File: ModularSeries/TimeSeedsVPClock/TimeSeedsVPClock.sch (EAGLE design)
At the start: 51 parts

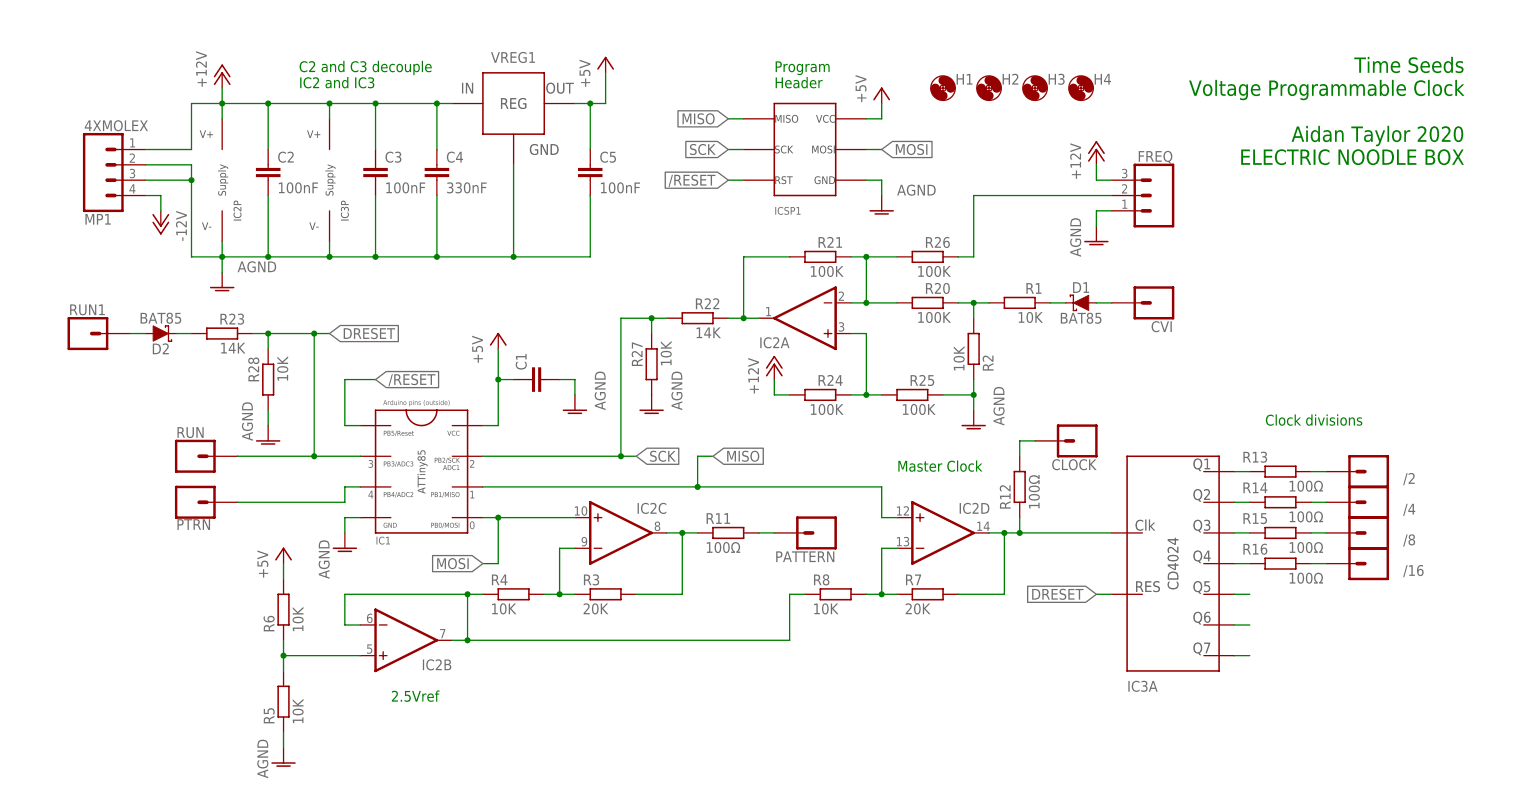
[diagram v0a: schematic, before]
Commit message: Schematic and layout added for Time Seeds and TRHP SVG
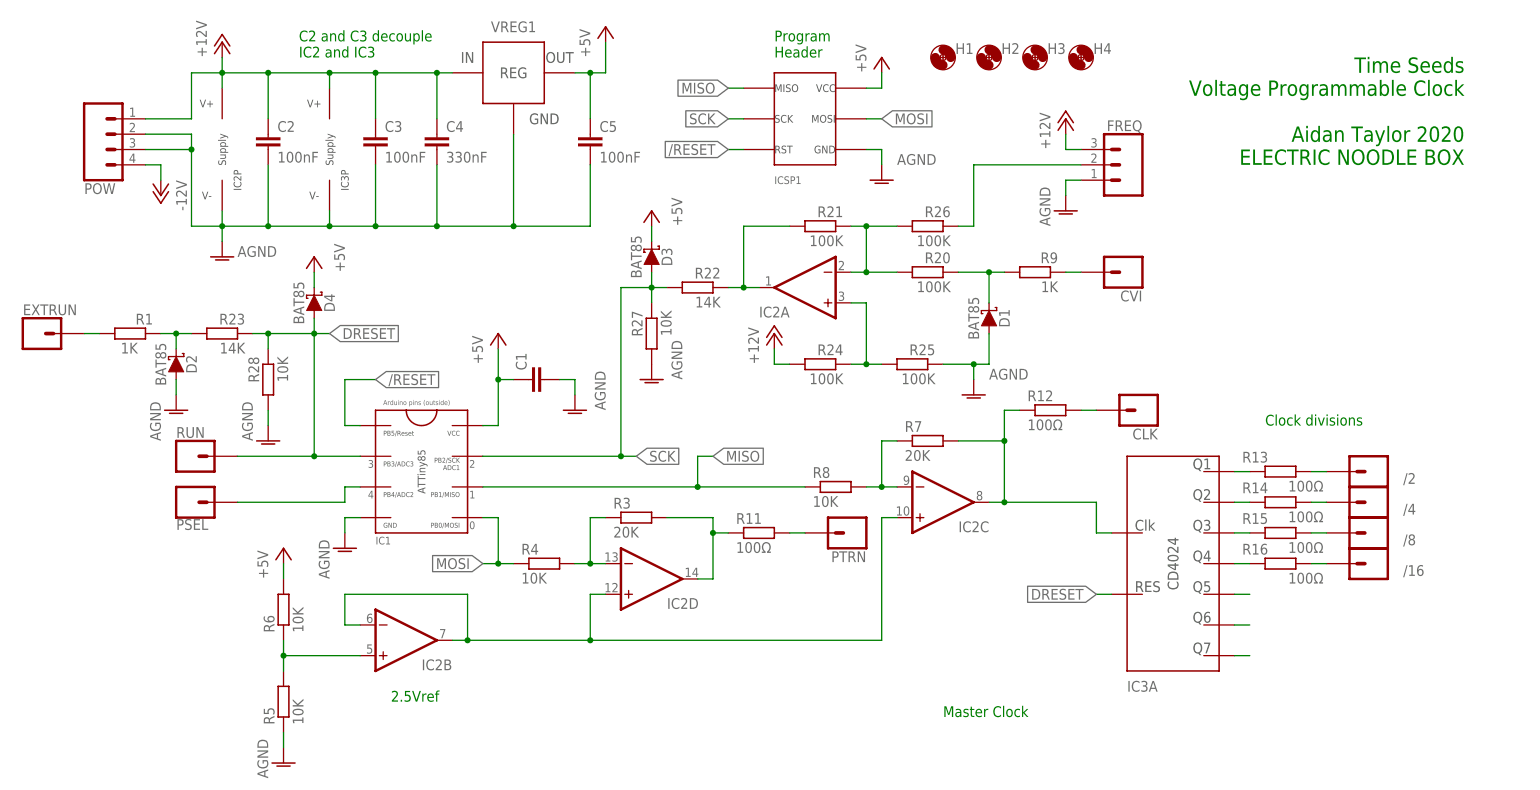
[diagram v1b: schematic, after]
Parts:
- removed CLOCK, PATTERN, RUN1: 1XWIREPAD, ElectricNoodleBox:1XWIREPAD
- removed MP1: 4XMOLEX, ElectricNoodleBox:4XMOLEX
- removed R2: 10K, rcl:R-EU_0207/10
- added CLK, EXTRUN, PSEL: 1XWIREPAD, ElectricNoodleBox:1XWIREPAD
- added D3, D4: BAT85, ElectricNoodleBox:SCHOTTKY_DO35
- added POW: 4XMOLEX, ElectricNoodleBox:4XMOLEX
- added R9: 1K, rcl:R-EU_0207/10
- IC2: device ElectricNoodleBox:TL0X4DIL -> ElectricNoodleBox:LM324
- R1: value 10K -> 1K
- VREG1: value L7805_TO-220 -> (none); device ElectricNoodleBox:L7805_TO-220 -> ElectricNoodleBox:L78L05TO92
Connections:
- removed net N$12: CLOCK.1, R12.2
- removed net N$26: D2.A, RUN1.1
- removed net N$28: D2.C, R23.2
- new net N$3: CVI.1, R9.1
- new net N$7: D2.C, R1.1, R23.2
- net +12V: now also POW.1; no longer MP1.1
- net +5V: now also D3.C, D4.C
- net -12V: now also POW.4; no longer MP1.4
- net AGND: now also D1.A, D2.A, POW.2, POW.3; no longer MP1.2, MP1.3, R2.1
- net DRESET: now also D4.A
- net MISO: now also R8.1; no longer IC2D.+IN
- net MOSI: now also R4.1; no longer IC2C.+IN
- net N$1: now also R20.1, R9.2; no longer R1.1
- net N$10: now also IC2C.+IN, IC2D.+IN; no longer R4.1, R8.1
- net N$11: now also PTRN.1; no longer PATTERN.1
- net N$2: now also EXTRUN.1; no longer R2.2, R20.1
- net N$23: now also CLK.1, R12.2; no longer CVI.1, D1.A
- net N$24: now also PSEL.1; no longer PTRN.1
- net N$4: now also IC2D.-IN; no longer IC2C.-IN
- net N$5: now also IC2D.OUT; no longer IC2C.OUT
- net N$8: now also IC2C.-IN; no longer IC2D.-IN
- net N$9: now also IC2C.OUT; no longer IC2D.OUT
- net SCK: now also D3.A
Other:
- moved on the sheet: C2, C3, C4, C5, CVI, D1, D2, FREQ, H1, H2, H3, H4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

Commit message: Time Seeds VPC and TRHP SVG op-amps, schematics and layouts updated
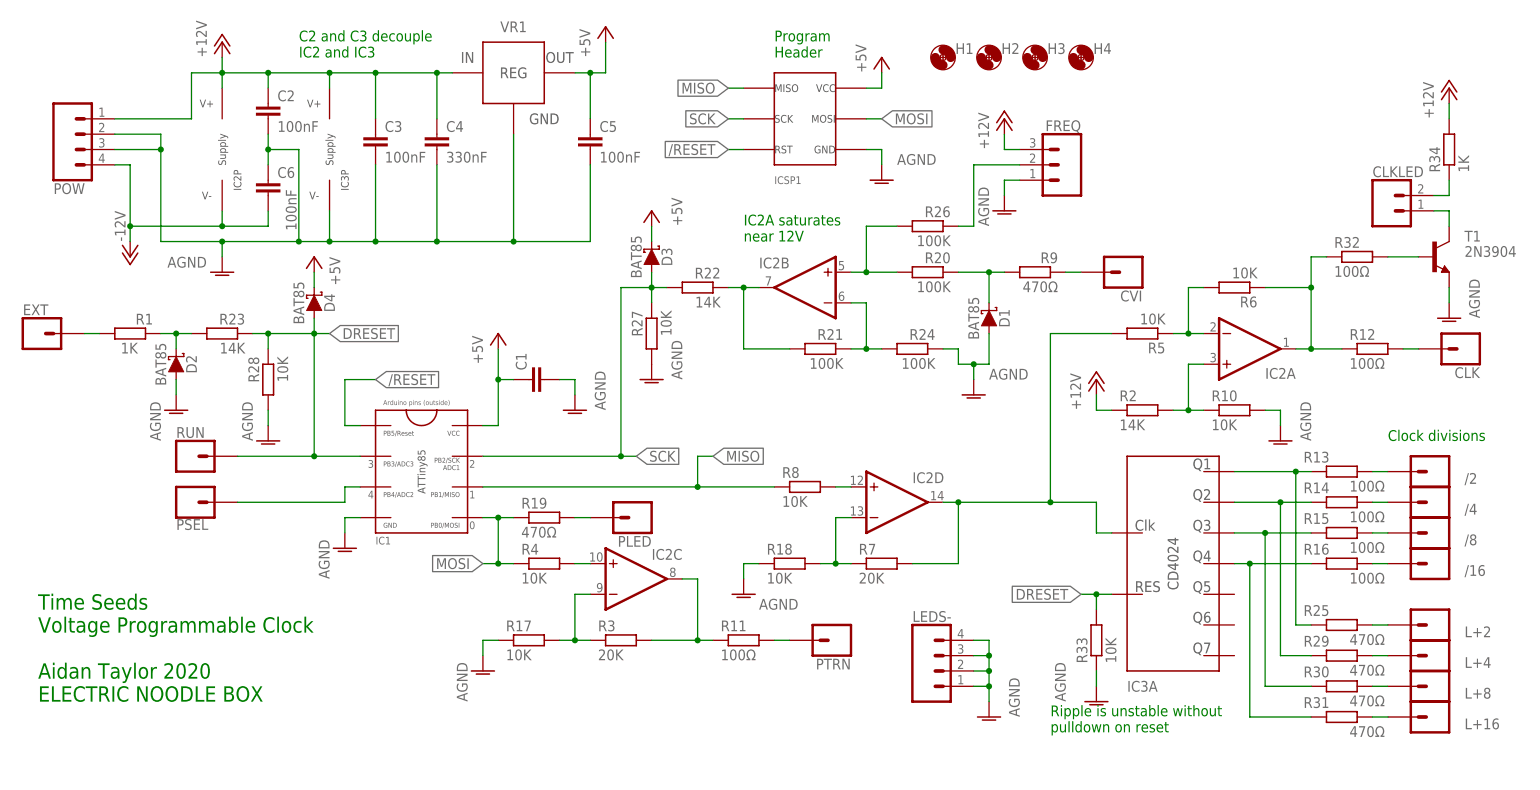
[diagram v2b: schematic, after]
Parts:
- added C6: 100nF, rcl:C-EU050-025X075
- added CLKLED: 2XWIREPAD, ElectricNoodleBox:2XWIREPAD
- added L+16, L+2, L+4, L+8, PLED: 1XWIREPAD, ElectricNoodleBox:1XWIREPAD
- added LEDS-: 4XWIREPAD, ElectricNoodleBox:4XWIREPAD
- added R10, R17, R18, R33: 10K, rcl:R-EU_0207/10
- added R19, R29, R30, R31: 470Ω, rcl:R-EU_0207/10
- added R2: 14K, rcl:R-EU_0207/10
- added R32: 100Ω, rcl:R-EU_0207/10
- added R34: 1K, rcl:R-EU_0207/10
- added T1: 2N3904, transistor:2N3904
- R25: value 100K -> 470Ω
- R9: value 1K -> 470Ω
- renumbered EXTRUN to EXT, VREG1 to VR1
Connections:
- new net N$12: IC2A.OUT, R12.1, R32.1, R6.1
- new net N$22: IC2A.+IN, R10.1, R2.2
- new net N$26: CLKLED.2, R34.1
- new net N$28: IC2D.-IN, R18.2, R7.1
- new net N$33: IC2D.OUT, IC3A.CLK, R5.2, R7.2
- new net N$34: L+16.1, R31.2
- new net N$35: CLKLED.1, T1.C
- new net N$36: R32.2, T1.B
- net +12V: now also R2.1, R34.2; no longer R24.2
- net +5V: no longer R6.2
- net -12V: now also C6.2, IC2P.V-
- net AGND: now also C6.1, LEDS-.1, LEDS-.2, LEDS-.3, LEDS-.4, R10.2, R17.1, R18.1, R24.1, R33.1, T1.E; no longer IC2P.V-, R25.1, R5.1
- net DRESET: now also R33.2
- net MOSI: now also R19.1
- net N$10: now also IC2C.OUT, R11.1, R3.2; no longer IC2B.-IN, IC2B.OUT, IC2C.+IN, IC2D.+IN
- net N$13: now also R25.1
- net N$14: now also R29.1
- net N$15: now also R30.1
- net N$16: now also R31.1
- net N$17: now also L+2.1, R25.2; no longer IC3A.Q5
- net N$18: now also L+4.1, R29.2; no longer IC3A.Q6
- net N$19: now also L+8.1, R30.2; no longer IC3A.Q7
- net N$20: now also IC2B.+IN; no longer IC2A.-IN, R21.1
- net N$21: now also IC2B.OUT; no longer IC2A.OUT
- net N$25: now also IC2B.-IN, R21.1, R24.2; no longer IC2A.+IN, R24.1, R25.2
- net N$4: now also IC2C.+IN; no longer IC2D.-IN, R3.1
- net N$5: now also IC2C.-IN, R17.2, R3.1; no longer IC2D.OUT, R11.1, R3.2
- net N$6: now also IC2A.-IN, R5.1, R6.2; no longer IC2B.+IN, R5.2, R6.1
- net N$8: now also IC2D.+IN; no longer IC2C.-IN, R7.1
- net N$9: now also PLED.1, R19.2; no longer IC2C.OUT, IC3A.CLK, R12.1, R7.2
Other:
- note added: "IC2A saturates near 12V"
- note added: "Ripple is unstable without pulldown on reset"
- note removed: "2.5Vref"
- note removed: "Master Clock"
- moved on the sheet: /16, /2, /4, /8, C2, CLK, FREQ, IC2A, IC2B, IC2C, IC2D, POW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

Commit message: CD4024 Reset fixed in Time Seeds
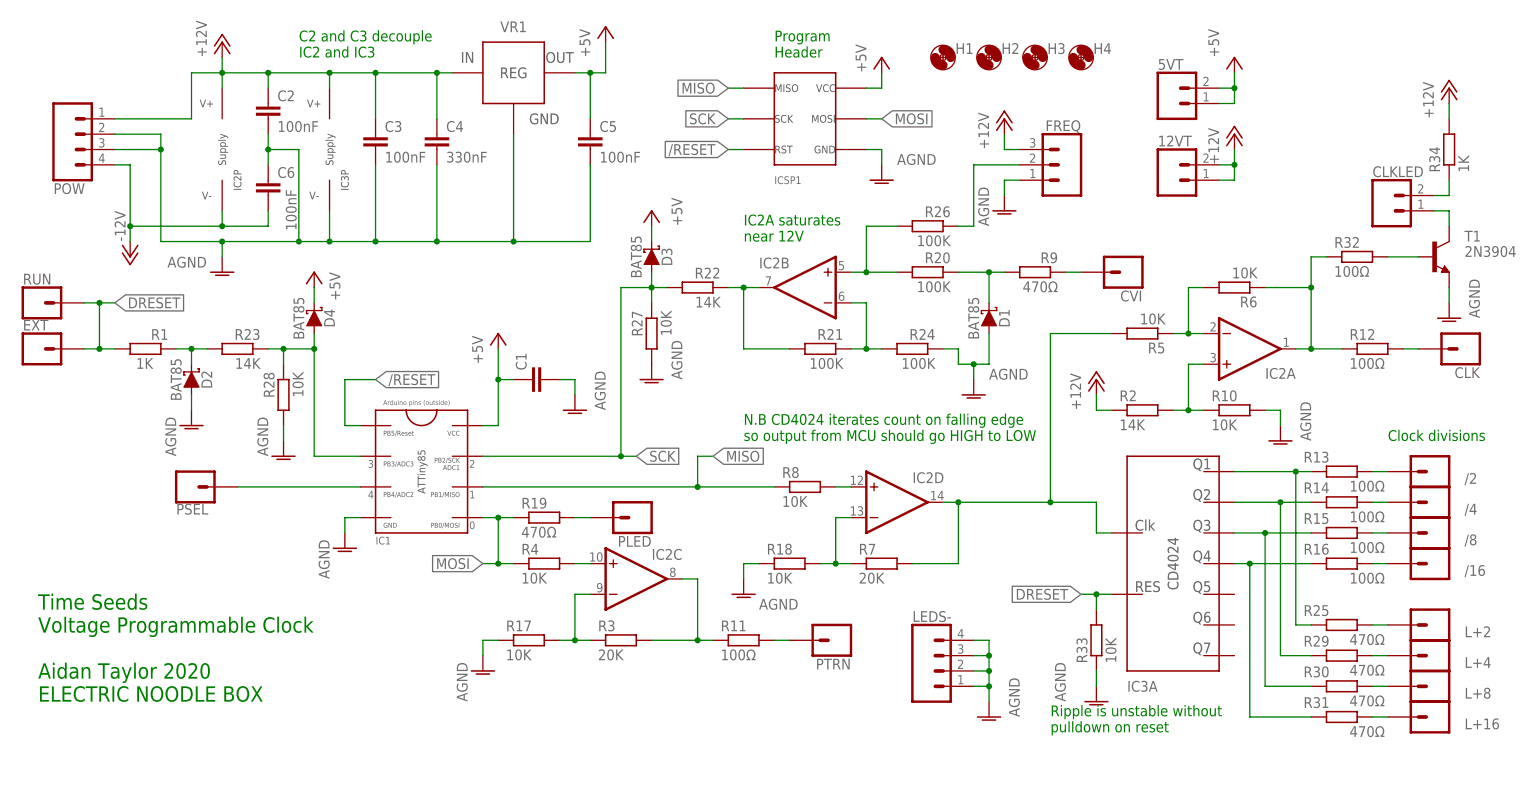
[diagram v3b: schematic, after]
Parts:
- added 12VT, 5VT: 2XWIREPAD, ElectricNoodleBox:2XWIREPAD
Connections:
- removed net N$2: EXT.1, R1.2
- new net NOTRES: D4.A, IC1.PB3, R23.1, R28.1
- net +12V: now also 12VT.1, 12VT.2
- net +5V: now also 5VT.1, 5VT.2
- net DRESET: now also EXT.1, R1.2; no longer D4.A, IC1.PB3, R23.1, R28.1
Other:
- note added: "N.B CD4024 iterates count on falling edge so output from MCU should go HIGH to LOW"
- moved on the sheet: D2, D4, EXT, PSEL, R1, R23, R28, RUN

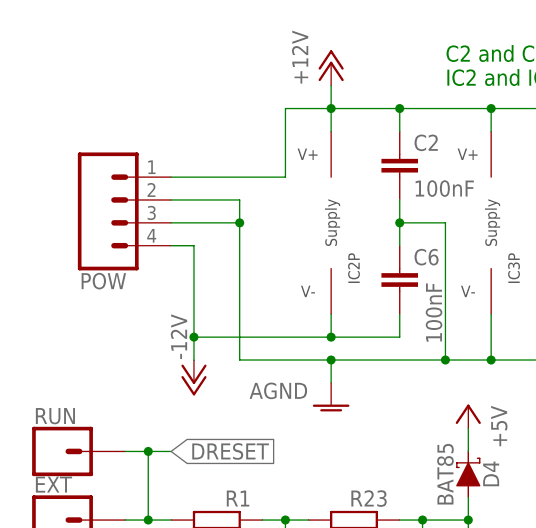
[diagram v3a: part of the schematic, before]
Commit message: Power header updated on most PCBs. Knives layout added
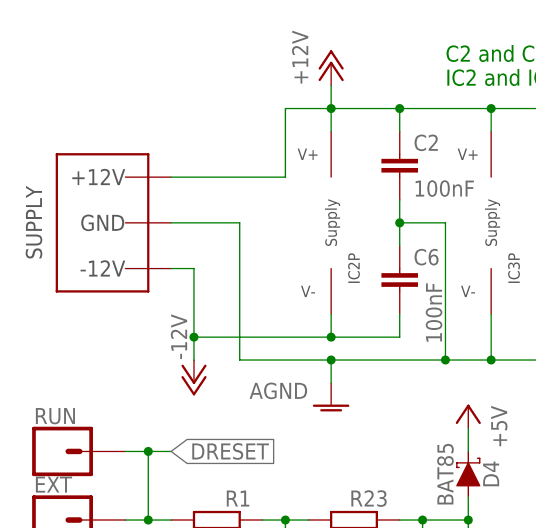
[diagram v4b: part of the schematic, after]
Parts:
- removed POW: 4XMOLEX, ElectricNoodleBox:4XMOLEX
- added WP1: COMBO_SUPPLY_HEADER, ElectricNoodleBox:COMBO_SUPPLY_HEADER
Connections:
- net +12V: now also WP1.V++; no longer POW.1
- net -12V: now also WP1.V--; no longer POW.4
- net AGND: now also WP1.AGND; no longer POW.2, POW.3
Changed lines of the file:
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@@
 <part name="C5" library="rcl" library_urn="urn:adsk.eagle:library:334" deviceset="C-EU" device="050-025X075" package3d_urn="urn:adsk.eagle:package:23637/1" value="100nF"/>
 <part name="P+7" library="supply1" library_urn="urn:adsk.eagle:library:371" deviceset="+5V" device=""/>
-<part name="POW" library="ElectricNoodleBox" deviceset="4XMOLEX" device=""/>
 <part name="P+4" library="supply1" library_urn="urn:adsk.eagle:library:371" deviceset="+5V" device=""/>
 <part name="AGND4" library="supply1" library_urn="urn:adsk.eagle:library:371" deviceset="AGND" device=""/>
@@
 <part name="5VT" library="ElectricNoodleBox" deviceset="2XWIREPAD" device=""/>
 <part name="12VT" library="ElectricNoodleBox" deviceset="2XWIREPAD" device=""/>
+<part name="WP1" library="ElectricNoodleBox" deviceset="COMBO_SUPPLY_HEADER" device=""/>
 </parts>
 <sheets>
@@
 <attribute name="VALUE" x="58.42" y="104.14" size="1.778" layer="96" rot="R90"/>
 </instance>
-<instance part="POW" gate="G$1" x="-25.4" y="91.44" smashed="yes" rot="MR180">
-<attribute name="NAME" x="-30.48" y="83.312" size="1.778" layer="95" font="vector" rot="MR180"/>
-</instance>
 <instance part="P+4" gate="1" x="106.68" y="104.14" smashed="yes">
 <attribute name="VALUE" x="104.14" y="101.6" size="1.778" layer="96" rot="R90"/>
@@
 <attribute name="NAME" x="152.4" y="89.408" size="1.778" layer="95" font="vector"/>
 </instance>
+<instance part="WP1" gate="G$1" x="-27.94" y="88.9" smashed="yes" rot="MR0"/>
 </instances>
 <busses>
@@
 <junction x="22.86" y="73.66"/>
 <junction x="33.02" y="73.66"/>
-<pinref part="POW" gate="G$1" pin="3"/>
 <wire x1="-20.32" y1="88.9" x2="-12.7" y2="88.9" width="0.1524" layer="91"/>
-<pinref part="POW" gate="G$1" pin="2"/>
-<wire x1="-20.32" y1="91.44" x2="-12.7" y2="91.44" width="0.1524" layer="91"/>
-<wire x1="-12.7" y1="91.44" x2="-12.7" y2="88.9" width="0.1524" layer="91"/>
-<junction x="-12.7" y="88.9"/>
 <wire x1="-12.7" y1="88.9" x2="-12.7" y2="73.66" width="0.1524" layer="91"/>
 <wire x1="-12.7" y1="73.66" x2="-2.54" y2="73.66" width="0.1524" layer="91"/>
@@
 <wire x1="-2.54" y1="73.66" x2="-2.54" y2="71.12" width="0.1524" layer="91"/>
 <junction x="-2.54" y="73.66"/>
+<pinref part="WP1" gate="G$1" pin="AGND"/>
 </segment>
 </net>
@@
 <wire x1="33.02" y1="101.6" x2="33.02" y2="93.98" width="0.1524" layer="91"/>
 <junction x="33.02" y="101.6"/>
-<pinref part="POW" gate="G$1" pin="1"/>
 <wire x1="-20.32" y1="93.98" x2="-7.62" y2="93.98" width="0.1524" layer="91"/>
 <wire x1="-7.62" y1="93.98" x2="-7.62" y2="101.6" width="0.1524" layer="91"/>
 <wire x1="-7.62" y1="101.6" x2="-2.54" y2="101.6" width="0.1524" layer="91"/>
+<pinref part="WP1" gate="G$1" pin="V++"/>
 </segment>
 <segment>
@@
 <net name="-12V" class="0">
 <segment>
-<pinref part="POW" gate="G$1" pin="4"/>
-<wire x1="-20.32" y1="86.36" x2="-17.78" y2="86.36" width="0.1524" layer="91"/>
+<wire x1="-20.32" y1="83.82" x2="-17.78" y2="83.82" width="0.1524" layer="91"/>
 <pinref part="P-1" gate="1" pin="-12V"/>
-<wire x1="-17.78" y1="86.36" x2="-17.78" y2="76.2" width="0.1524" layer="91"/>
+<wire x1="-17.78" y1="83.82" x2="-17.78" y2="76.2" width="0.1524" layer="91"/>
 <pinref part="C6" gate="G$1" pin="2"/>
 <wire x1="-17.78" y1="76.2" x2="-17.78" y2="73.66" width="0.1524" layer="91"/>
@@
 <wire x1="-2.54" y1="78.74" x2="-2.54" y2="76.2" width="0.1524" layer="91"/>
 <junction x="-2.54" y="76.2"/>
-</segment>
-</net>
+<pinref part="WP1" gate="G$1" pin="V--"/>
+</segment>
+</net>

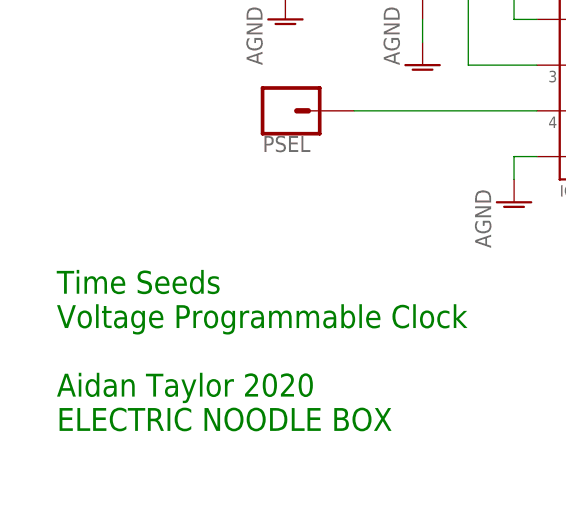
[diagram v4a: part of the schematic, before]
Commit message: BOM, panel wiring and documentation complete for TimeSeed
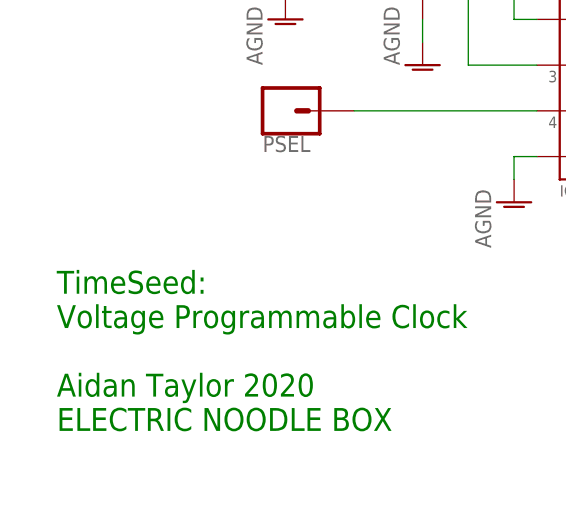
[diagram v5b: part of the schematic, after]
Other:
- note added: "TimeSeed: Voltage Programmable Clock Aidan Taylor 2020 ELECTRIC NOODLE BOX"
- note removed: "Time Seeds Voltage Programmable Clock Aidan Taylor 2020 ELECTRIC NOODLE BOX"
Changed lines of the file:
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@@
 IC2 and IC3</text>
 <text x="190.5" y="40.64" size="1.778" layer="91">Clock divisions</text>
-<text x="-33.02" y="-2.54" size="2.54" layer="91">Time Seeds
+<text x="-33.02" y="-2.54" size="2.54" layer="91">TimeSeed:
 Voltage Programmable Clock
 Aidan Taylor 2020
